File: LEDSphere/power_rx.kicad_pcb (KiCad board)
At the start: 2 copper layers, 140 x 140 mm, 51 parts, among them U114 DRV5033FAQDBZR, U3 TPS54202HDDCR, U4 TPS54202HDDCR

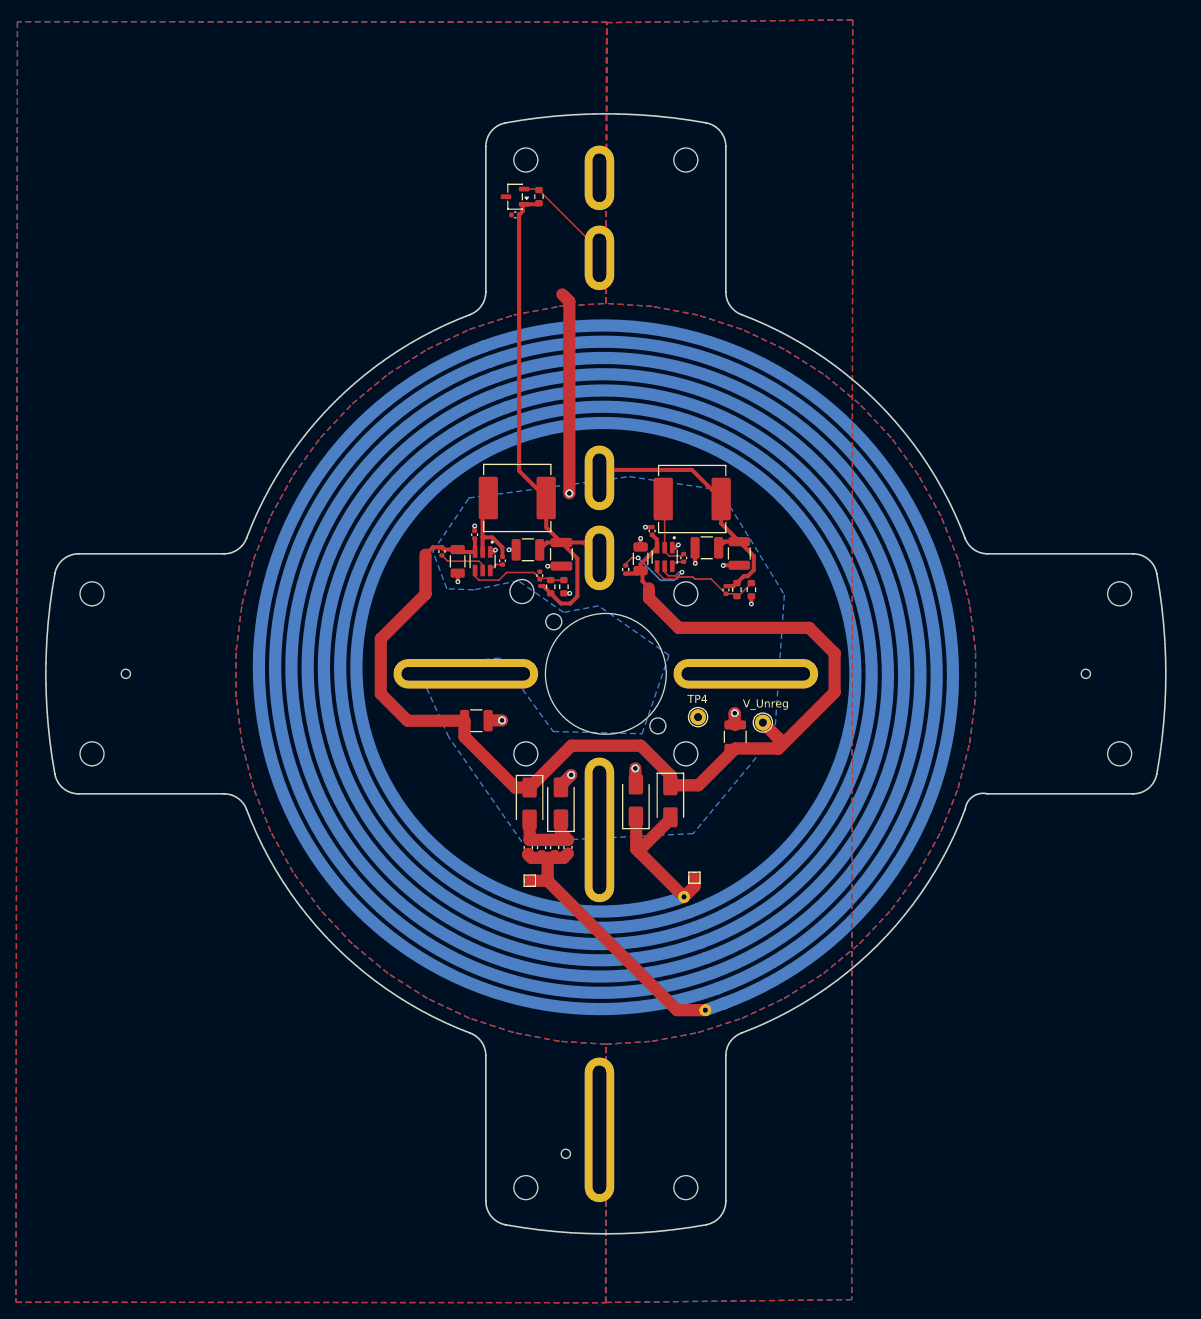
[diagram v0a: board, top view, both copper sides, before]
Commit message: alter rx to avoid flux lines
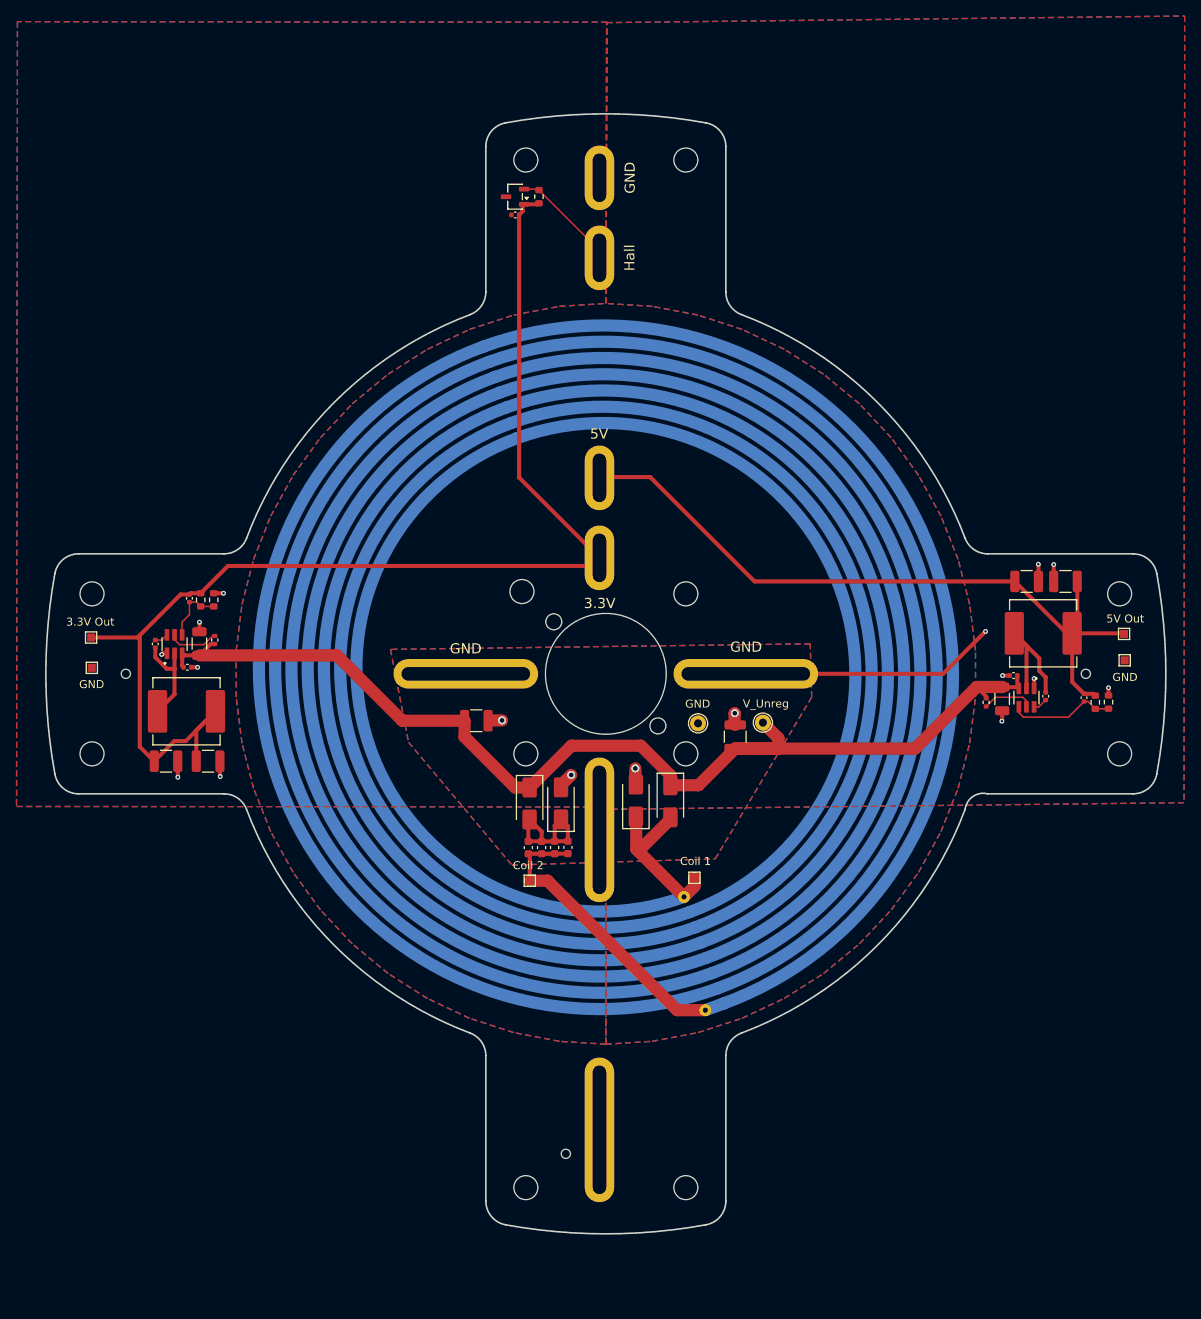
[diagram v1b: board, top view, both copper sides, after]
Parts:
- added TP5: 5V, TestPoint:TestPoint_Pad_1.0x1.0mm, F.Cu at (159.3, 99.3)
- added TP6: 3.3V, TestPoint:TestPoint_Pad_1.0x1.0mm, F.Cu at (30.1, 99.7)
- added TP7: GND, TestPoint:TestPoint_Pad_1.0x1.0mm, F.Cu at (30.2, 103.5)
- added TP8: GND, TestPoint:TestPoint_Pad_1.0x1.0mm, F.Cu at (159.3, 102.6)
- moved C13 52.4 mm to (39.5, 115.2), turned to 180 degrees
- moved C15 51.2 mm to (44.8, 115.2), turned to 180 degrees
- moved L2 49.2 mm to (42.1, 109.0)
- moved C4 48.7 mm to (145.4, 104.5), turned to 0 degrees
- moved U4 48.5 mm to (147.1, 107.3)
- moved C2 48.5 mm to (144.0, 107.4), turned to 90 degrees
- moved C11 48.4 mm to (149.5, 107.1)
- moved R2 48.0 mm to (142.0, 107.8), turned to 90 degrees
- moved L3 47.0 mm to (149.2, 99.2)
- moved R5 47.0 mm to (155.7, 107.8)
- moved R6 46.8 mm to (157.3, 107.8), turned to -90 degrees
- moved C18 46.7 mm to (154.3, 107.3)
- moved C16 45.0 mm to (151.9, 92.7)
- moved C10 44.6 mm to (38.2, 100.5), turned to 90 degrees
- moved C17 43.9 mm to (42.4, 94.8), turned to 90 degrees
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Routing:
- net +3.3V: track 68.8 -> 152.1 mm
- net +5V: track 34.9 -> 90.2 mm
- net GND: track 45.8 -> 55.7 mm
- net Net-(U4-SW): track 9.33 -> 16.5 mm
- net /U_unreg: track 147.3 -> 140.2 mm
- net Net-(D1-A): track 10.3 -> 17.3 mm
- net Net-(U4-EN): track 12.4 -> 6.44 mm, vias 2 -> 0
- net Net-(U3-FB): track 12.8 -> 7.75 mm
- net /coil2: track 37.0 -> 39.3 mm
- net Net-(U4-FB): track 14.7 -> 13.4 mm
- net Net-(U3-SW): track 11.2 -> 12.3 mm
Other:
- board text added: "3.3V"
- board text added: "3.3V Out"
- board text added: "5V"
- board text added: "5V Out"
- board text added: "Coil 1"
- board text added: "Coil 2"
- board text added: "GND"
- board text added: "Hall"

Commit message: add leds
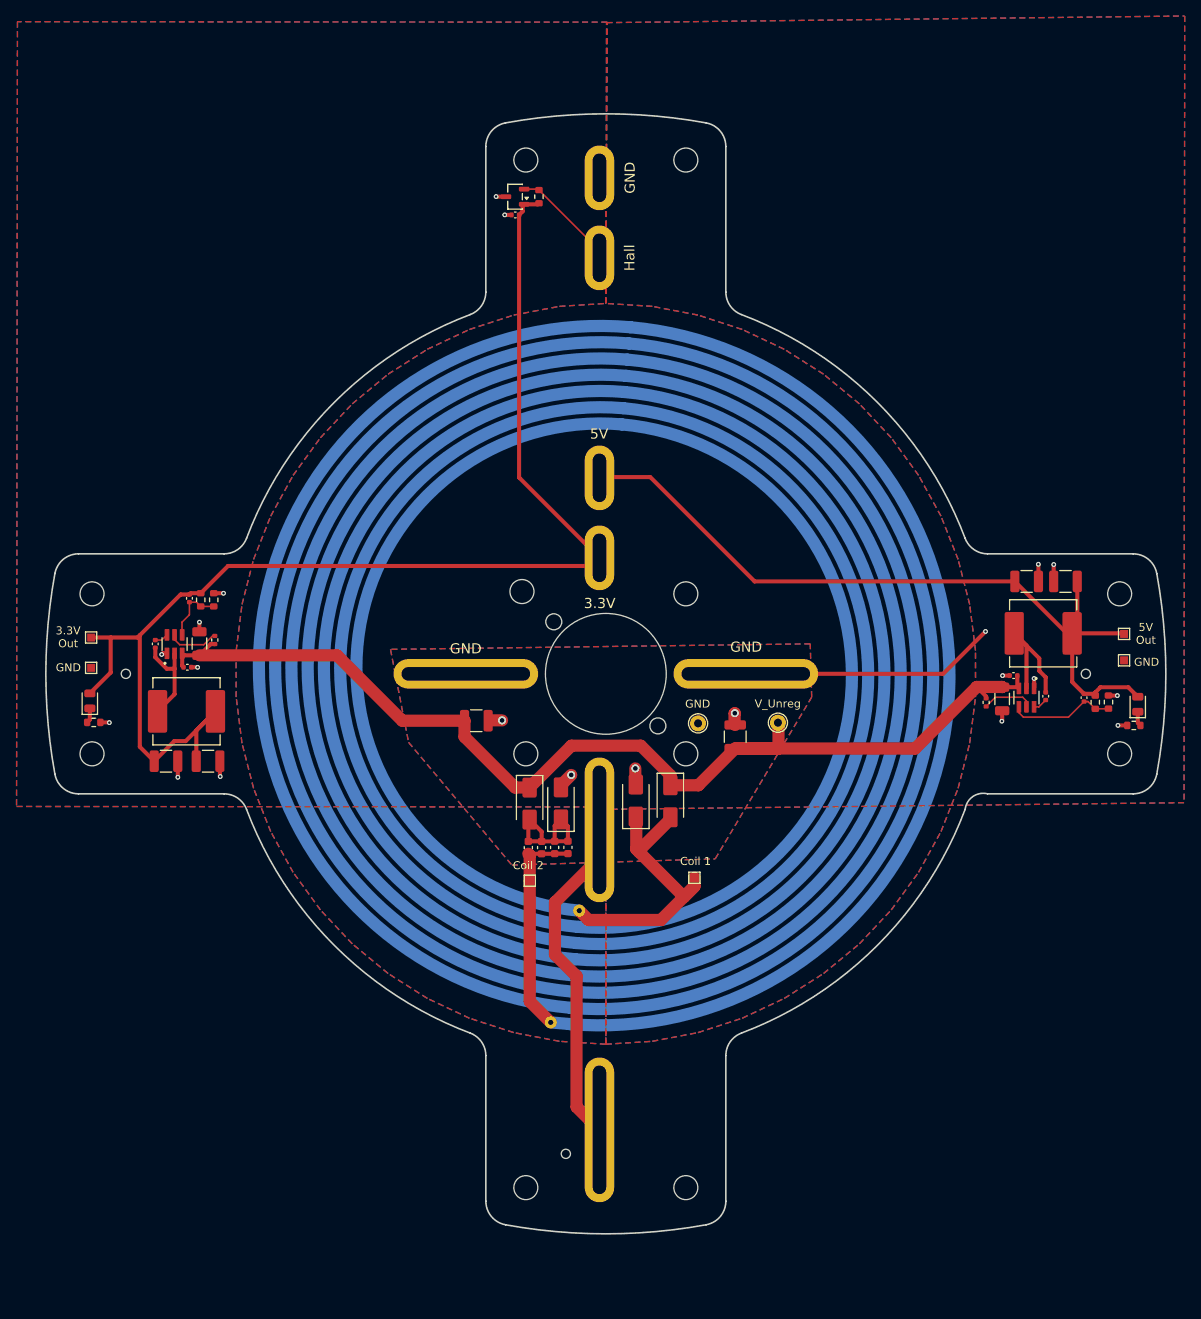
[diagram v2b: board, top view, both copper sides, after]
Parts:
- added D5: LED, LED_SMD:LED_0805_2012Metric, F.Cu at (30.0, 107.7)
- added D6: LED, LED_SMD:LED_0805_2012Metric, F.Cu at (161.0, 108.1)
- added R8: 1k, Resistor_SMD:R_0603_1608Metric, F.Cu at (30.5, 110.3)
- added R9: 1k, Resistor_SMD:R_0603_1608Metric, F.Cu at (160.5, 110.7)
- moved TP3 1.88 mm to (116.0, 110.4)
- moved TP7 0.09 mm to (30.1, 103.5)
- moved TP8 0.07 mm to (159.3, 102.6)
- turned REF** to -95 degrees
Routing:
- net GND: track 55.7 -> 102.4 mm, vias 17 -> 21
- net /coil1: track 21.4 -> 38.0 mm
- net /coil2: track 39.3 -> 27.2 mm
- net +3.3V: track 152.1 -> 160.2 mm
- net +5V: track 90.2 -> 96.6 mm
- net Net-(D5-K): track 0.00 -> 1.89 mm
- net Net-(D6-K): track 0.00 -> 1.85 mm
- net /U_unreg: track 140.2 -> 139.4 mm

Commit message: FINAL PUSHES
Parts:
- added G***: LOGO, LOGO, F.Cu at (119.8, 75.5)
- added G***: LOGO, LOGO, F.Cu at (67.6, 131.7)
- added G***: LOGO, LOGO, F.Cu at (119.8, 131.7)
- added G***: LOGO, LOGO, F.Cu at (67.6, 75.5)
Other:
- board text added: "Designed by: Ellen Sun"
- board text added: "Eclectronics SP'26 Ellen Sun Jun Park"
- board text added: "LED SPHERE RX BOARD"

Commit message: update
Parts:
- moved R7 6.36 mm to (88.7, 50.5)
- moved C19 6.36 mm to (85.7, 52.7)
- moved U114 6.36 mm to (85.7, 50.5)
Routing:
- net +3.3V: track 160.2 -> 153.3 mm
- net Hall: track 18.5 -> 13.0 mm
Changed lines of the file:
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@@
 	(footprint "Capacitor_SMD:C_0402_1005Metric"
 		(layer "F.Cu")
-		(at 83.17 46.915 180)
+		(at 85.735 52.73 180)
 		(descr "Capacitor SMD 0402 (1005 Metric), square (rectangular) end terminal, IPC-7351 nominal, (Body size source: IPC-SM-782 page 76, https://www.pcb-3d.com/wordpress/wp-content/uploads/ipc-sm-782a_amendment_1_and_2.pdf)")
 		(tags "capacitor")
@@
 	(footprint "Package_TO_SOT_SMD:SOT-23-3"
 		(layer "F.Cu")
-		(at 83.1425 44.64 180)
+		(at 85.7075 50.455 180)
 		(descr "SOT, 3 Pin (JEDEC MO-178 inferred 3-pin variant https://www.jedec.org/document_search?search_api_views_fulltext=MO-178)")
 		(tags "SOT TO_SOT_SMD")
@@
 	(footprint "Resistor_SMD:R_0603_1608Metric"
 		(layer "F.Cu")
-		(at 86.13 44.635 90)
+		(at 88.695 50.45 90)
 		(descr "Resistor SMD 0603 (1608 Metric), square (rectangular) end terminal, IPC-7351 nominal, (Body size source: IPC-SM-782 page 72, https://www.pcb-3d.com/wordpress/wp-content/uploads/ipc-sm-782a_amendment_1_and_2.pdf)")
 		(tags "resistor")
@@
 		)
 		(fp_arc
-			(start 36.602998 -0.000002)
-			(mid 0.000002 36.602998)
-			(end -36.602998 0.000002)
+			(start 36.602998 -0.000003)
+			(mid 0.000003 36.602998)
+			(end -36.602998 0.000003)
 			(stroke
 				(width 1.524)
@@
 			(start -34.571998 -0.000002)
 			(mid 1.015499 -35.586999)
-			(end 36.602998 -0.000002)
+			(end 36.602998 -0.000003)
 			(stroke
 				(width 1.524)
@@
 		)
 		(fp_arc
-			(start -36.602998 0.000002)
+			(start -36.602998 0.000003)
 			(mid 1.015997 -37.618999)
 			(end 38.635 0)
@@
 		(fp_arc
 			(start -40.667 0.000002)
-			(mid 1.015997 -41.682998)
+			(mid 1.015996 -41.682998)
 			(end 42.699 -0.000003)
 			(stroke
@@
 	)
 	(segment
-		(start 86 45.59)
-		(end 84.28 45.59)
+		(start 88.565 51.405)
+		(end 86.845 51.405)
 		(width 0.508)
 		(layer "F.Cu")
@@
 	)
 	(segment
-		(start 84.1 45.77)
-		(end 84.1 46.465)
+		(start 86.665 51.585)
+		(end 86.665 52.28)
 		(width 0.508)
 		(layer "F.Cu")
@@
 	)
 	(segment
-		(start 84.1 46.465)
-		(end 83.65 46.915)
+		(start 86.665 52.28)
+		(end 86.215 52.73)
 		(width 0.508)
 		(layer "F.Cu")
@@
 	)
 	(segment
-		(start 83.65 79.74)
-		(end 93.69 89.78)
+		(start 35.96 99.74)
+		(end 36.23 99.47)
 		(width 0.508)
 		(layer "F.Cu")
@@
 	)
 	(segment
-		(start 35.96 99.74)
-		(end 36.23 99.47)
+		(start 86.215 82.305)
+		(end 93.69 89.78)
 		(width 0.508)
 		(layer "F.Cu")
@@
 	)
 	(segment
-		(start 84.28 45.59)
-		(end 84.1 45.77)
+		(start 86.845 51.405)
+		(end 86.665 51.585)
 		(width 0.508)
 		(layer "F.Cu")
@@
 	)
 	(segment
-		(start 83.65 46.915)
-		(end 83.65 79.74)
+		(start 86.215 52.73)
+		(end 86.215 82.305)
 		(width 0.508)
 		(layer "F.Cu")
@@
 	)
 	(segment
-		(start 86.13 45.46)
-		(end 86 45.59)
+		(start 88.695 51.275)
+		(end 88.565 51.405)
 		(width 0.508)
 		(layer "F.Cu")
@@
 	)
 	(segment
-		(start 82.005 44.64)
-		(end 80.79 44.64)
+		(start 84.57 50.455)
+		(end 83.355 50.455)
 		(width 0.508)
 		(layer "F.Cu")
@@
 	)
 	(segment
-		(start 80.79 44.64)
-		(end 80.77 44.62)
+		(start 83.355 50.455)
+		(end 83.335 50.435)
 		(width 0.508)
 		(layer "F.Cu")
@@
 	)
 	(segment
-		(start 82.69 46.915)
-		(end 81.855 46.915)
+		(start 85.255 52.73)
+		(end 84.42 52.73)
 		(width 0.508)
 		(layer "F.Cu")
@@
 	)
 	(segment
-		(start 81.855 46.915)
-		(end 81.85 46.91)
+		(start 84.42 52.73)
+		(end 84.415 52.725)
 		(width 0.508)
 		(layer "F.Cu")
@@
 	)
 	(via
-		(at 80.77 44.62)
+		(at 83.335 50.435)
 		(size 0.6)
 		(drill 0.3)
@@
 	)
 	(via
-		(at 81.85 46.91)
+		(at 84.415 52.725)
 		(size 0.6)
 		(drill 0.3)
@@
 	)
 	(segment
-		(start 86.01 43.69)
-		(end 86.13 43.81)
+		(start 88.695 49.625)
+		(end 91.035 49.625)
+		(width 0.2)
+		(layer "F.Cu")
+		(net "Hall")
+	)
+	(segment
+		(start 88.575 49.505)
+		(end 88.695 49.625)
 		(width 0.2)
 		(layer "F.Cu")
@@
 	)
 	(segment
-		(start 84.1 43.665)
-		(end 84.125 43.69)
+		(start 86.665 49.48)
+		(end 86.69 49.505)
 		(width 0.2)
 		(layer "F.Cu")
@@
 	)
 	(segment
-		(start 86.13 43.81)
-		(end 93.69 51.37)
-		(width 0.2)
-		(layer "F.Cu")
-		(net "Hall")
-	)
-	(segment
 		(start 94.49 52.28)
 		(end 94.49 56.113622)
@@
 	)
 	(segment
-		(start 84.125 43.69)
-		(end 86.01 43.69)
+		(start 86.69 49.505)
+		(end 88.575 49.505)
 		(width 0.2)
 		(layer "F.Cu")
@@
 	)
 	(segment
-		(start 93.69 51.37)
+		(start 91.035 49.625)
 		(end 93.69 52.28)
 		(width 0.2)
